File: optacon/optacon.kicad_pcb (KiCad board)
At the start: 2 copper layers, 61.9 x 90.9 mm, 18 parts, among them J1 Conn_01x12, U1 HV528, U2 HV528, U3 DRV2665

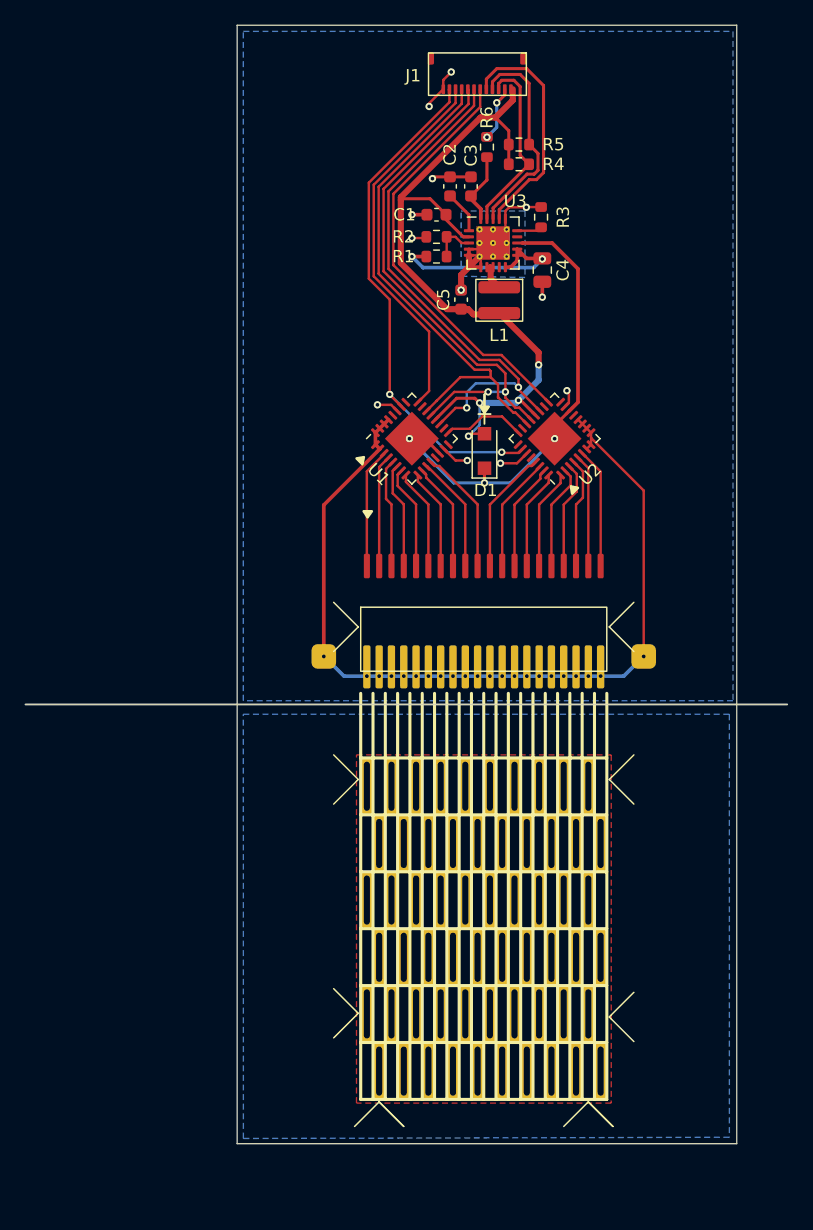
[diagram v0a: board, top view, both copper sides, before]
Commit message: add test points, mounting holes
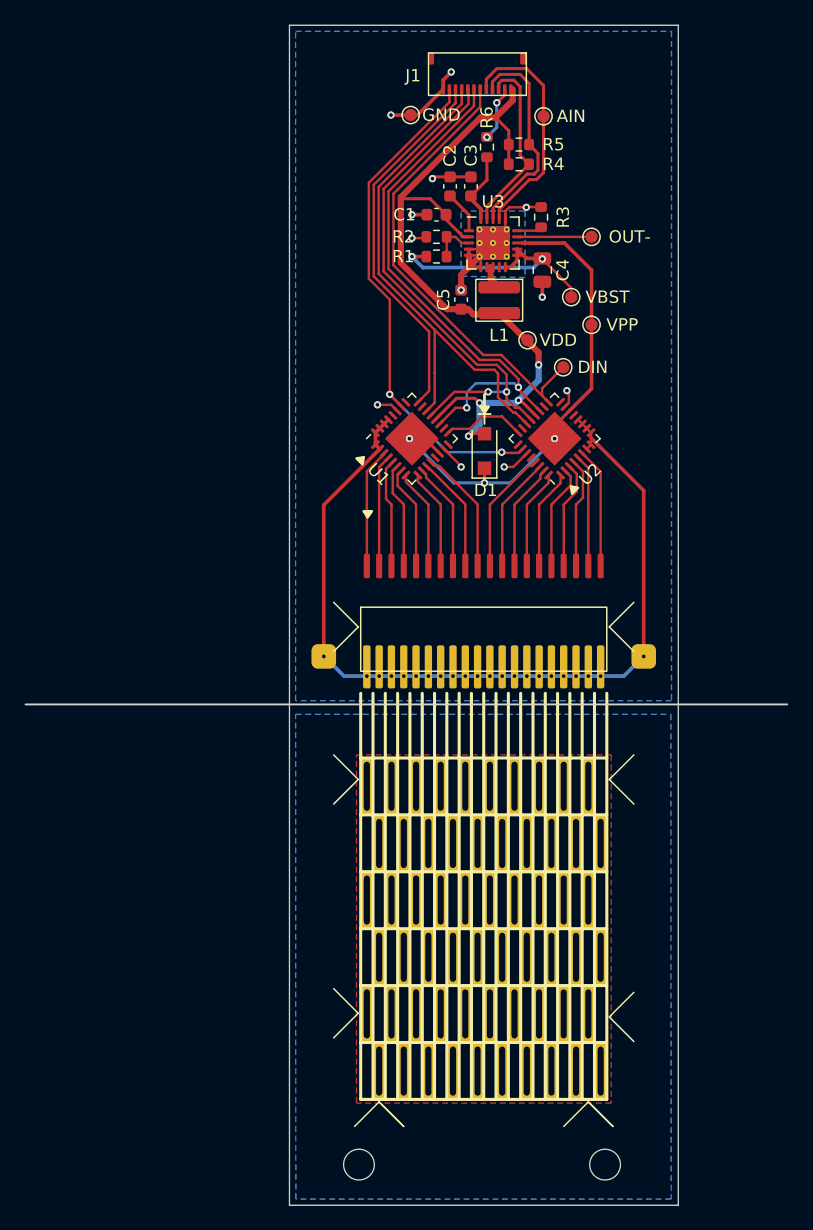
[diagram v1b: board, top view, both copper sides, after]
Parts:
- added AIN: TestPoint, TestPoint:TestPoint_Pad_D1.0mm, F.Cu at (109.0, 47.8)
- added DIN: TestPoint, TestPoint:TestPoint_Pad_D1.0mm, F.Cu at (110.6, 68.2)
- added GND: TestPoint, TestPoint:TestPoint_Pad_D1.0mm, F.Cu at (98.2, 47.7)
- added OUT-: TestPoint, TestPoint:TestPoint_Pad_D1.0mm, F.Cu at (112.9, 57.6)
- added REF**: MountingHole_2.5mm, MountingHole:MountingHole_2.5mm, F.Cu at (94.0, 133.0)
- added REF**: MountingHole_2.5mm, MountingHole:MountingHole_2.5mm, F.Cu at (114.0, 133.0)
- added VBST: TestPoint, TestPoint:TestPoint_Pad_D1.0mm, F.Cu at (111.2, 62.5)
- added VDD: TestPoint, TestPoint:TestPoint_Pad_D1.0mm, F.Cu at (107.7, 66.0)
- added VPP: TestPoint, TestPoint:TestPoint_Pad_D1.0mm, F.Cu at (112.9, 64.8)
- L1: value VLS3012HBX-3R3M -> 3.3 µH
- piezo1: value Conn_01x21 -> Conn_01x22
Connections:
- net /hv_driver/VBST renamed /VBST
- U3 pad 14: /hv_driver/OUT- -> /OUT-
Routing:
- net /OUT-: track 0.00 -> 6.04 mm
- net /VBST: track 16.9 -> 21.0 mm
- net /DIN: track 34.4 -> 37.5 mm
- net GND: track 32.8 -> 35.6 mm
- net /VPP: track 38.9 -> 40.4 mm
- net /LE: track 42.1 -> 42.9 mm
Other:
- board size 61.9 x 90.9 mm -> 61.9 x 95.9 mm
- board text added: "piezo driver board rev 2.1"
- board text removed: "piezo driver board rev 2"

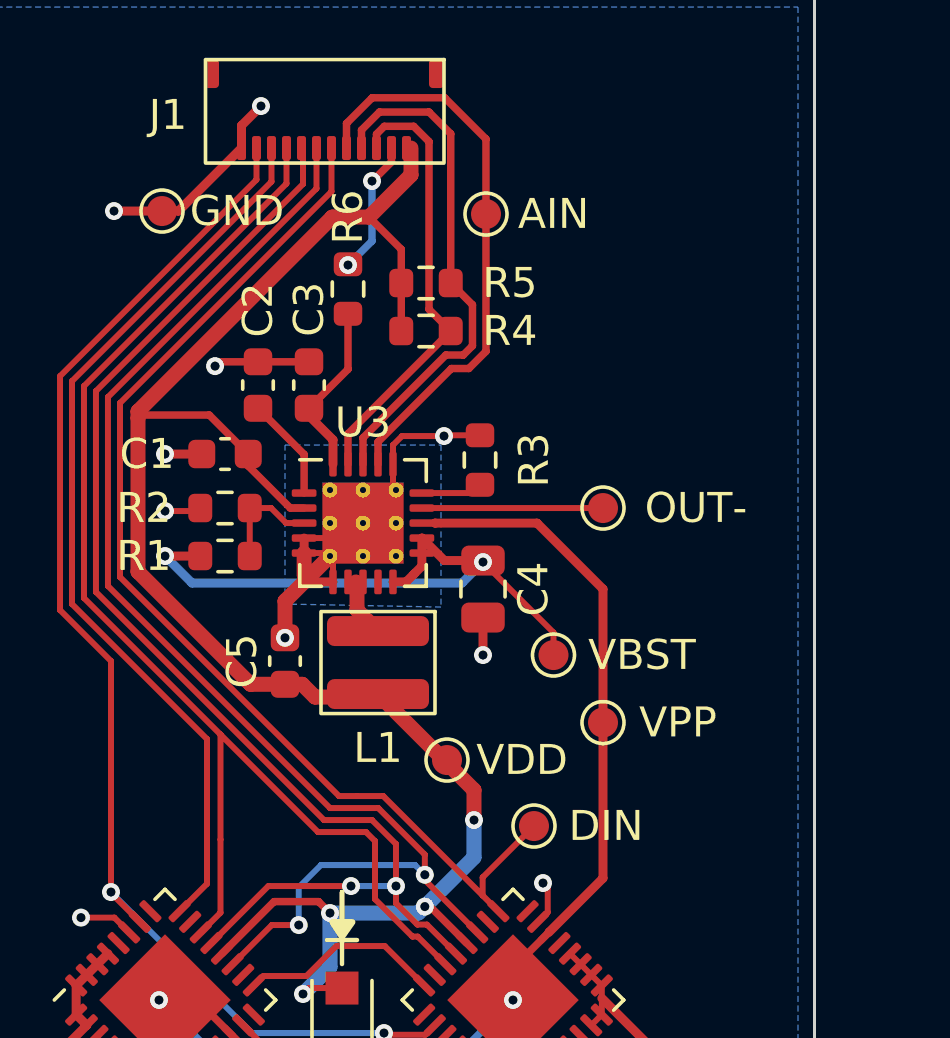
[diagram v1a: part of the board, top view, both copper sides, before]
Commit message: hierarchical sheet for shift registers
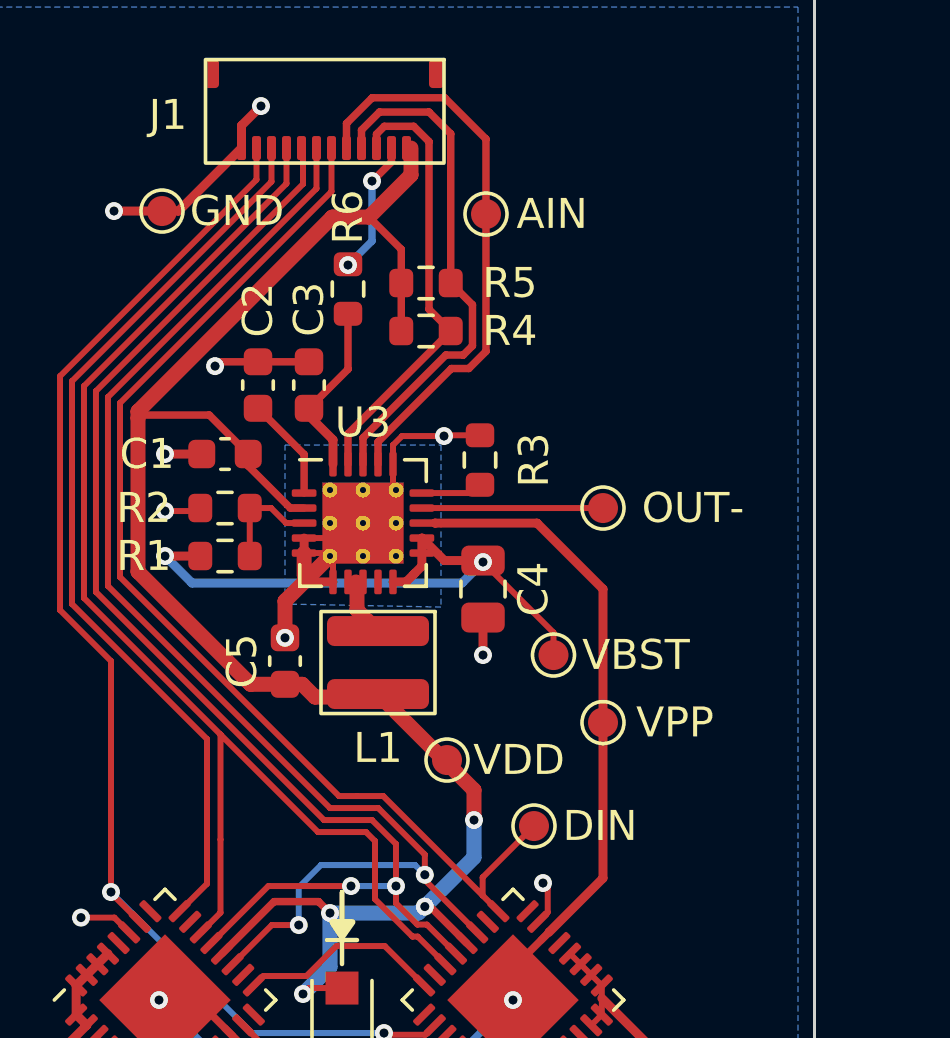
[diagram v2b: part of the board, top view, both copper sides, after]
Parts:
- renumbered VDD to TP1, GND to TP2, VPP to TP3, VBST to TP4, OUT- to TP5, AIN to TP6, DIN to TP7
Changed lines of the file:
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@@
     (descr "HVQFN, 32 Pin (https://www.nxp.com/docs/en/package-information/SOT617-1.pdf), generated with kicad-footprint-generator ipc_noLead_generator.py")
     (tags "HVQFN NoLead")
-    (property "Sheetfile" "optacon.kicad_sch")
-    (property "Sheetname" "")
+    (property "Sheetfile" "shift_registers.kicad_sch")
+    (property "Sheetname" "shift_registers")
     (attr smd)
     (fp_text reference "U1" (at -3.959798 0.141421 315 unlocked) (layer "F.SilkS")
@@
     (descr "HVQFN, 32 Pin (https://www.nxp.com/docs/en/package-information/SOT617-1.pdf), generated with kicad-footprint-generator ipc_noLead_generator.py")
     (tags "HVQFN NoLead")
-    (property "Sheetfile" "optacon.kicad_sch")
-    (property "Sheetname" "")
+    (property "Sheetfile" "shift_registers.kicad_sch")
+    (property "Sheetname" "shift_registers")
     (attr smd)
     (fp_text reference "U2" (at -4.101219 0 225) (layer "F.SilkS")
@@
     (property "Sheetname" "")
     (attr exclude_from_pos_files)
-    (fp_text reference "VBST" (at 2.95 0) (layer "F.SilkS")
+    (fp_text reference "TP4" (at 2.95 0) (layer "F.SilkS") hide
       (effects (font (size 1 1) (thickness 0.15)))
     )
     (fp_text value "TestPoint" (at 0 1.55) (layer "F.Fab")
+      (effects (font (size 1 1) (thickness 0.15)))
+    )
+    (fp_text user "VBST" (at 2.75 0 unlocked) (layer "F.SilkS")
       (effects (font (size 1 1) (thickness 0.15)))
     )
@@
     (property "Sheetname" "")
     (attr exclude_from_pos_files)
-    (fp_text reference "DIN" (at 2.4 0) (layer "F.SilkS")
+    (fp_text reference "TP7" (at 2.4 0) (layer "F.SilkS") hide
       (effects (font (size 1 1) (thickness 0.15)))
     )
     (fp_text value "TestPoint" (at 0 1.55) (layer "F.Fab")
+      (effects (font (size 1 1) (thickness 0.15)))
+    )
+    (fp_text user "DIN" (at 2.2 0 unlocked) (layer "F.SilkS")
       (effects (font (size 1 1) (thickness 0.15)))
     )
@@
     (property "Sheetname" "")
     (attr exclude_from_pos_files)
-    (fp_text reference "AIN" (at 2.25 0) (layer "F.SilkS")
+    (fp_text reference "TP6" (at 2.25 0) (layer "F.SilkS") hide
       (effects (font (size 1 1) (thickness 0.15)))
     )
     (fp_text value "TestPoint" (at 0 1.55) (layer "F.Fab")
+      (effects (font (size 1 1) (thickness 0.15)))
+    )
+    (fp_text user "AIN" (at 2.2 0 unlocked) (layer "F.SilkS")
       (effects (font (size 1 1) (thickness 0.15)))
     )
@@
     (property "Sheetname" "")
     (attr exclude_from_pos_files)
-    (fp_text reference "GND" (at 2.5 0) (layer "F.SilkS")
+    (fp_text reference "TP2" (at 2.5 0) (layer "F.SilkS") hide
       (effects (font (size 1 1) (thickness 0.15)))
     )
     (fp_text value "TestPoint" (at 0 1.55) (layer "F.Fab")
+      (effects (font (size 1 1) (thickness 0.15)))
+    )
+    (fp_text user "GND" (at 2.5 0 unlocked) (layer "F.SilkS")
       (effects (font (size 1 1) (thickness 0.15)))
     )
@@
     (property "Sheetname" "")
     (attr exclude_from_pos_files)
-    (fp_text reference "OUT-" (at 3.1 0) (layer "F.SilkS")
+    (fp_text reference "TP5" (at 3.1 0) (layer "F.SilkS") hide
       (effects (font (size 1 1) (thickness 0.15)))
     )
     (fp_text value "TestPoint" (at 0 1.55) (layer "F.Fab")
+      (effects (font (size 1 1) (thickness 0.15)))
+    )
+    (fp_text user "OUT-" (at 3 0 unlocked) (layer "F.SilkS")
       (effects (font (size 1 1) (thickness 0.15)))
     )
@@
     (property "Sheetname" "")
     (attr exclude_from_pos_files)
-    (fp_text reference "VDD" (at 2.5 0) (layer "F.SilkS")
+    (fp_text reference "TP1" (at 2.5 0) (layer "F.SilkS") hide
       (effects (font (size 1 1) (thickness 0.15)))
     )
     (fp_text value "TestPoint" (at 0 1.55) (layer "F.Fab")
+      (effects (font (size 1 1) (thickness 0.15)))
+    )
+    (fp_text user "VDD" (at 2.4 0 unlocked) (layer "F.SilkS")
       (effects (font (size 1 1) (thickness 0.15)))
     )
@@
     (tags "D_SOD-123F")
     (property "Part" " DSK120-K120")
-    (property "Sheetfile" "optacon.kicad_sch")
-    (property "Sheetname" "")
+    (property "Sheetfile" "shift_registers.kicad_sch")
+    (property "Sheetname" "shift_registers")
     (attr smd)
     (fp_text reference "D1" (at -3.2 0.1 180) (layer "F.SilkS")
@@
     (property "Sheetname" "")
     (attr exclude_from_pos_files)
-    (fp_text reference "VPP" (at 2.5 0) (layer "F.SilkS")
+    (fp_text reference "TP3" (at 2.5 0) (layer "F.SilkS") hide
       (effects (font (size 1 1) (thickness 0.15)))
     )
@@
       (effects (font (size 1 1) (thickness 0.15)))
     )
+    (fp_text user "VPP" (at 2.4 0 unlocked) (layer "F.SilkS")
+      (effects (font (size 1 1) (thickness 0.15)))
+    )
